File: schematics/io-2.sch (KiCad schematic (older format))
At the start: 8 parts, among them J13 FDC Connector, J13 Left Audio, J14 Right Audio, J9 IDE Connector, U11 WD1772, U12 EN5503DOC

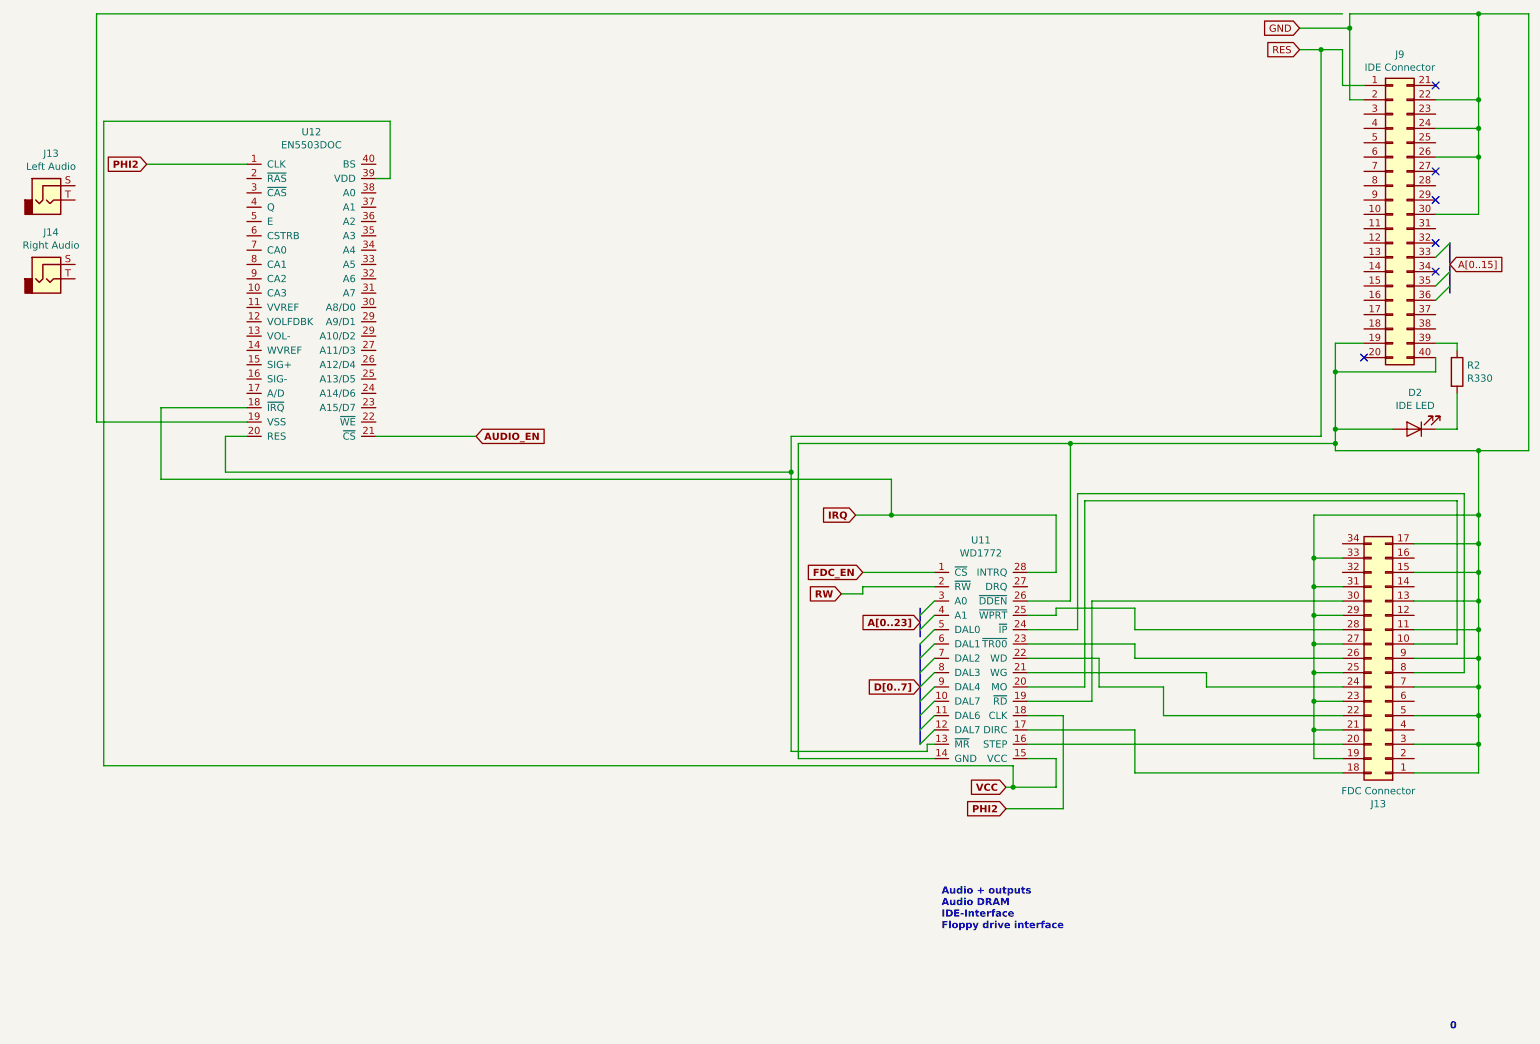
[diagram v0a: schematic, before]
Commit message: Added 8bit to 16bit IDE data handling latching.
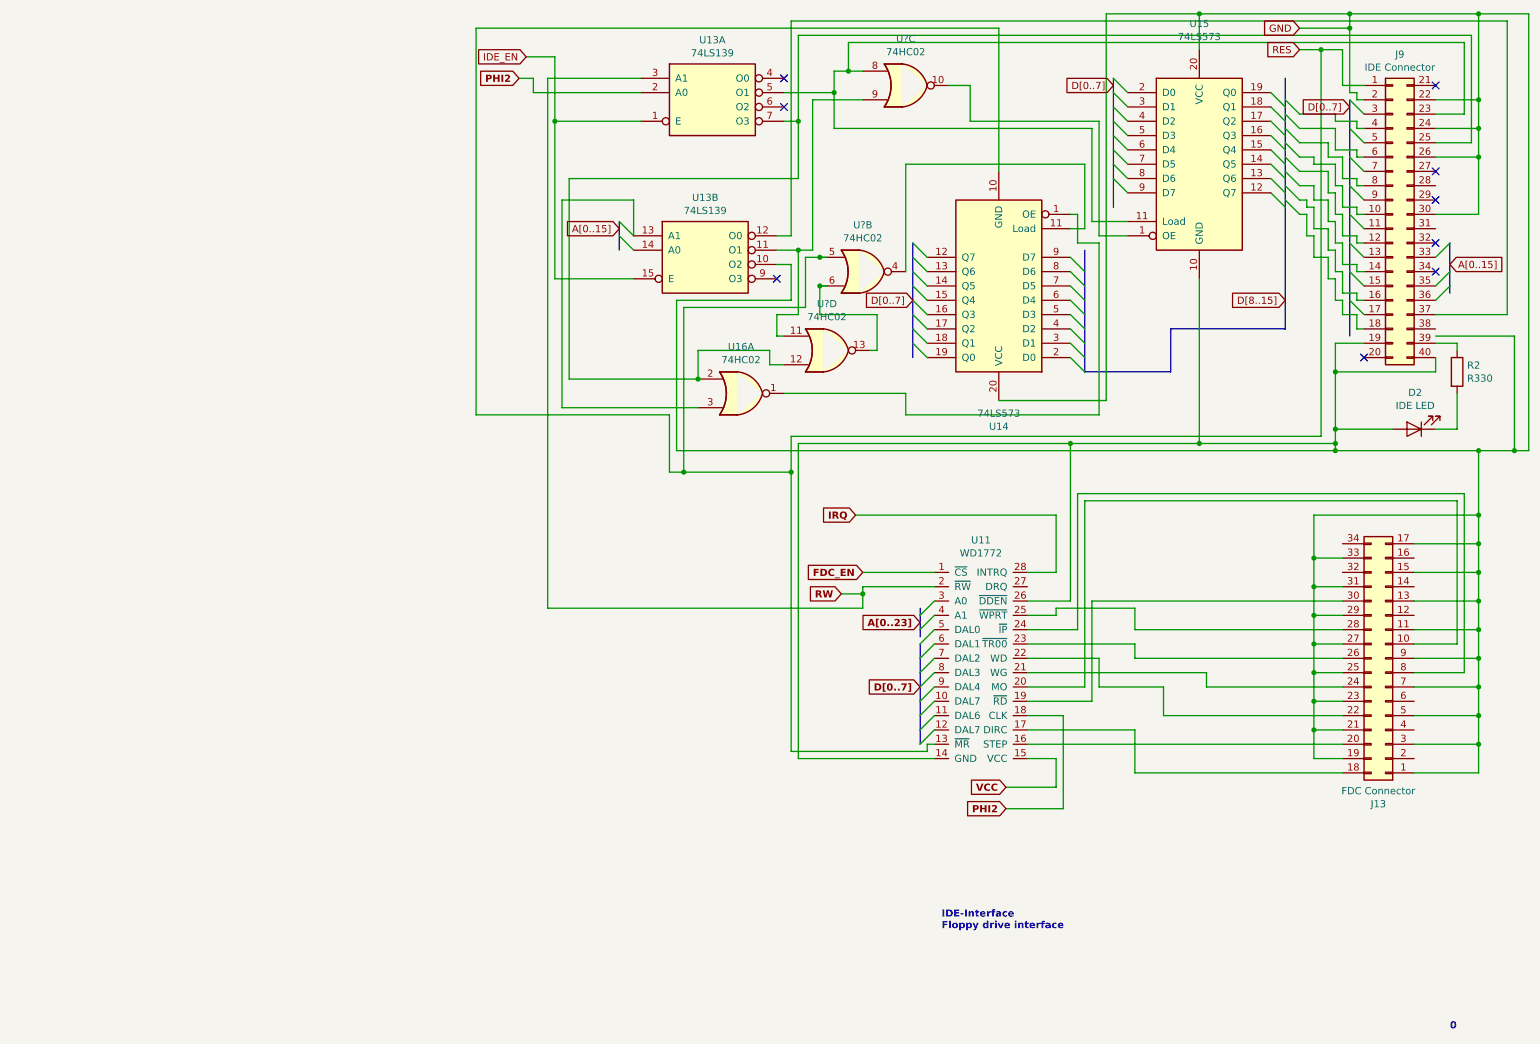
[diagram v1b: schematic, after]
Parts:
- removed J13: Left Audio, symbol Connector:AudioJack2
- removed J14: Right Audio, symbol Connector:AudioJack2
- removed U12: EN5503DOC, symbol prometh_custom:EN5503DOC
- added U13: 74LS139, symbol 74xx:74LS139
- added U14, U15: 74LS573, symbol 74xx:74LS573
- added U16, U? (x3): 74HC02, symbol 74xx:74HC02
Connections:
- net GND: now also U13.10 (O2), U14.20 (VCC), U15.10 (GND), U15.20 (VCC)
- net PHI2: now also U13.2 (A0)
- net RES: now also U14.10 (GND), U?.5
- net RW: now also U13.3 (A1)
- net at J9.23 (Pin_23): now also U13.5 (O1), U15.11 (Load), U?.8
- net at J9.25 (Pin_25): now also U13.7 (O3), U16.2, U?.12
- net at J9.37 (Pin_37): now also U13.12 (O0)
- new net: U15.1 (OE), U?.10
- new net: U14.1 (OE), U16.1
- new net: U14.11 (Load), U?.4
- new net: U13.11 (O1), U?.11, U?.9
- new net: U13.13 (A1), U16.3
- new net: U?.13, U?.6
- new net IDE_EN: U13.1 (E), U13.15 (E)
- no-connect marks 6 -> 9
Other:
- note added: "IDE-Interface\nFloppy drive interface"
- note removed: "Audio + outputs\nAudio DRAM\nIDE-Interface\nFloppy drive interface"

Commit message: merge from Jani's commit
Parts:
- removed U13: 74LS139, symbol 74xx:74LS139
- removed U14, U15: 74LS573, symbol 74xx:74LS573
- removed U16, U? (x3): 74HC02, symbol 74xx:74HC02
- added J13: Left Audio, symbol Connector:AudioJack2
- added J14: Right Audio, symbol Connector:AudioJack2
- added U12: EN5503DOC, symbol prometh_custom:EN5503DOC
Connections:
- net IRQ: now also U12.18 (~IRQ)
- net PHI2: now also U12.1 (CLK)
- net RES: now also U12.20 (RES)
- net VCC: now also U12.39 (VDD)
- new net AUDIO_EN: U12.21 (~CS)
- no-connect marks 9 -> 6
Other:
- note added: "Audio + outputs\nAudio DRAM\nIDE-Interface\nFloppy drive interface"
- note removed: "IDE-Interface\nFloppy drive interface"
